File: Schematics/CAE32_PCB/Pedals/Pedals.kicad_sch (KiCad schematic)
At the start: 20 parts, among them J1 Conn_01x19_Pin, SW1 CONFIG, SW2 SW, SW3 SW, U1 STM32F072RBTx, Y1 Crystal_GND24_Small

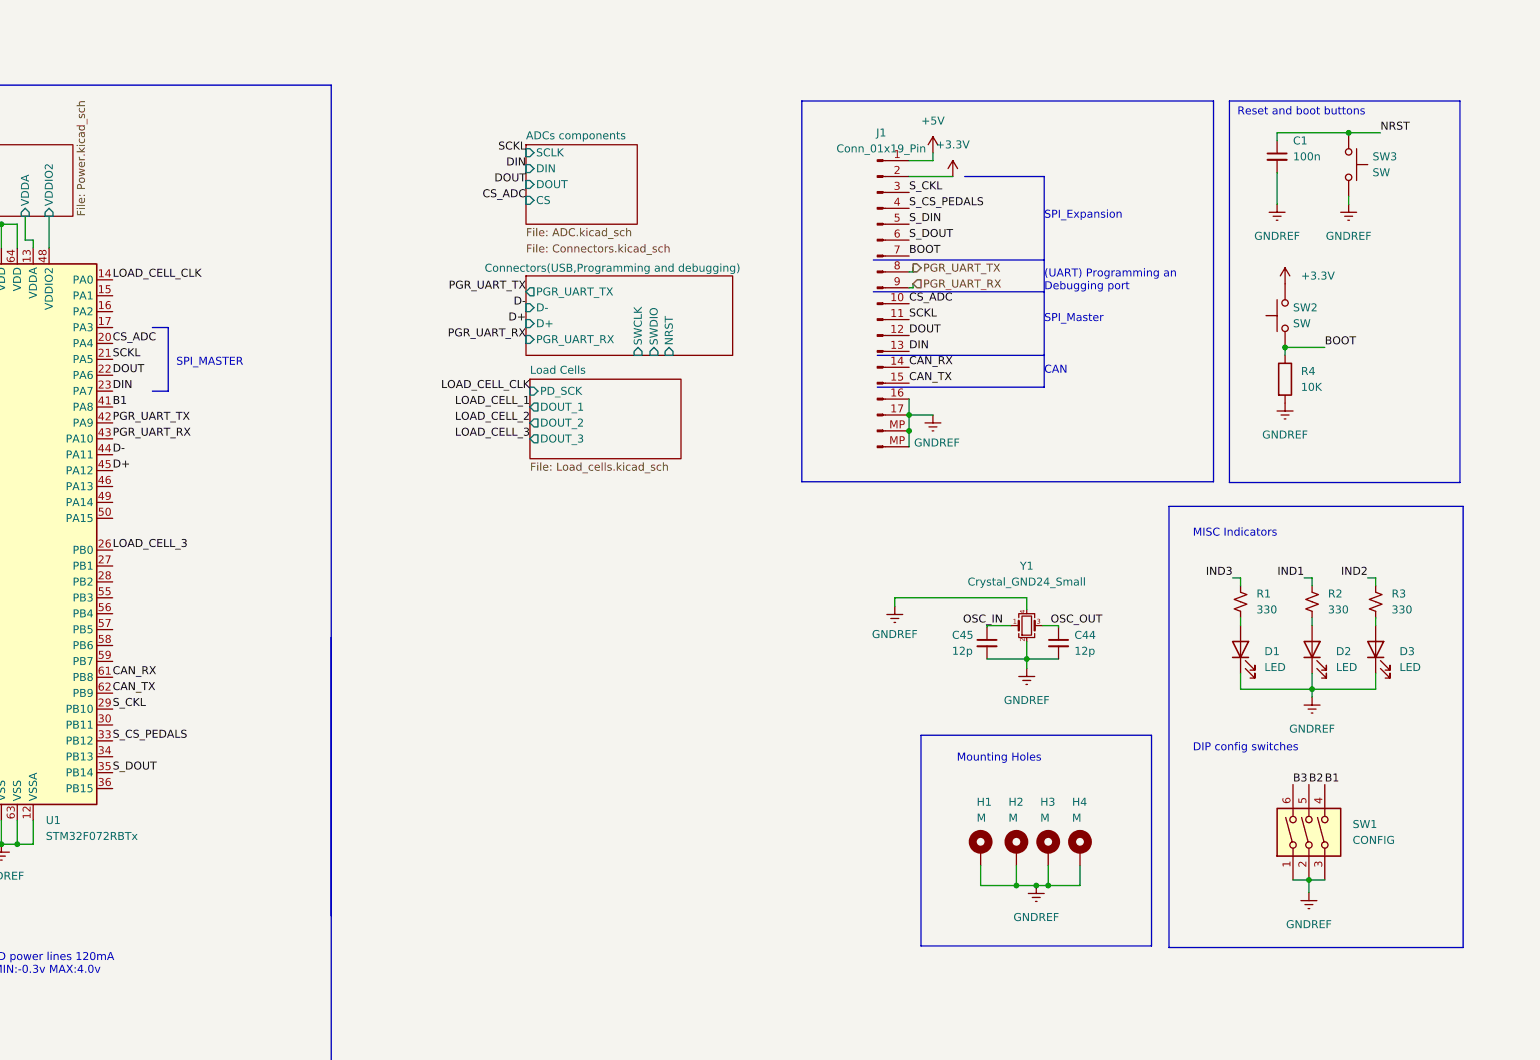
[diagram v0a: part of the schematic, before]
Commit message: updated: Pcb design, fixed plane grounds and minor improvements, added stlink connector, updated BOM with the current market stock
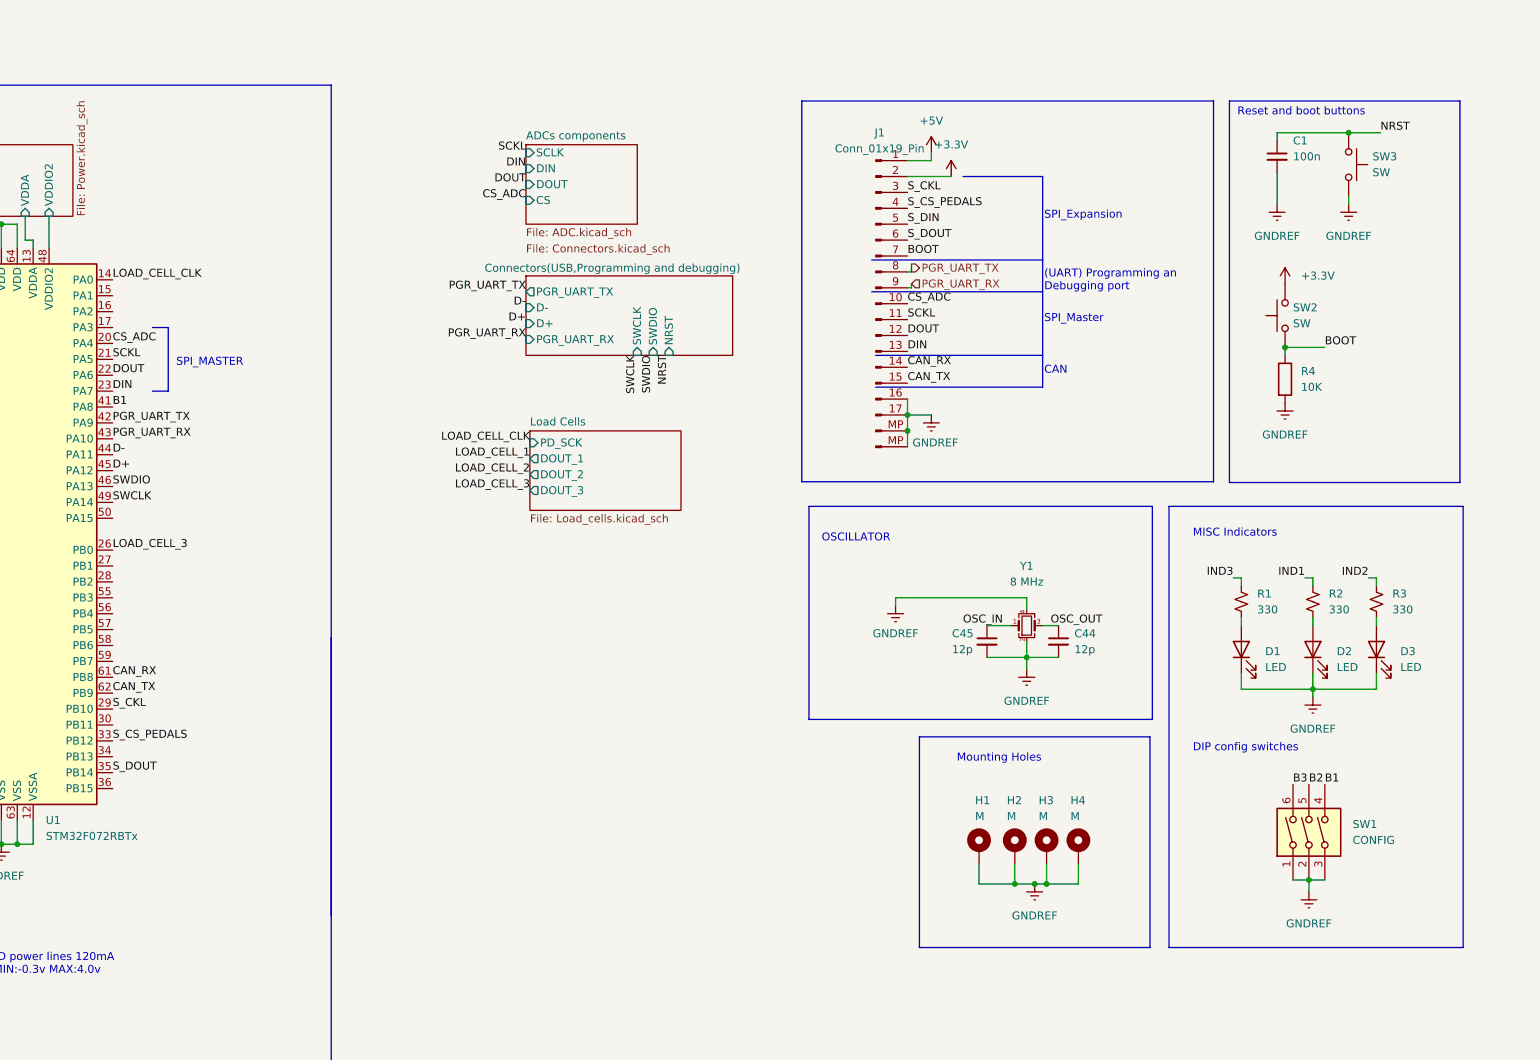
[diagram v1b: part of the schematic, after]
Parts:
- C1: Item c1591 -> C66501; LCSC_PART c1591 -> C66501; Vendor c1591 -> C66501
- R1, R2, R3: Item C25804 -> C21190; LCSC_PART C25804 -> C21190; Vendor C25804 -> C21190
- Y1: value Crystal_GND24_Small -> 8 MHz
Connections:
- net SWDIO: now reaches U1.46 (PA13)
- net SWCLK: now reaches U1.49 (PA14)
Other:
- note added: "OSCILLATOR"

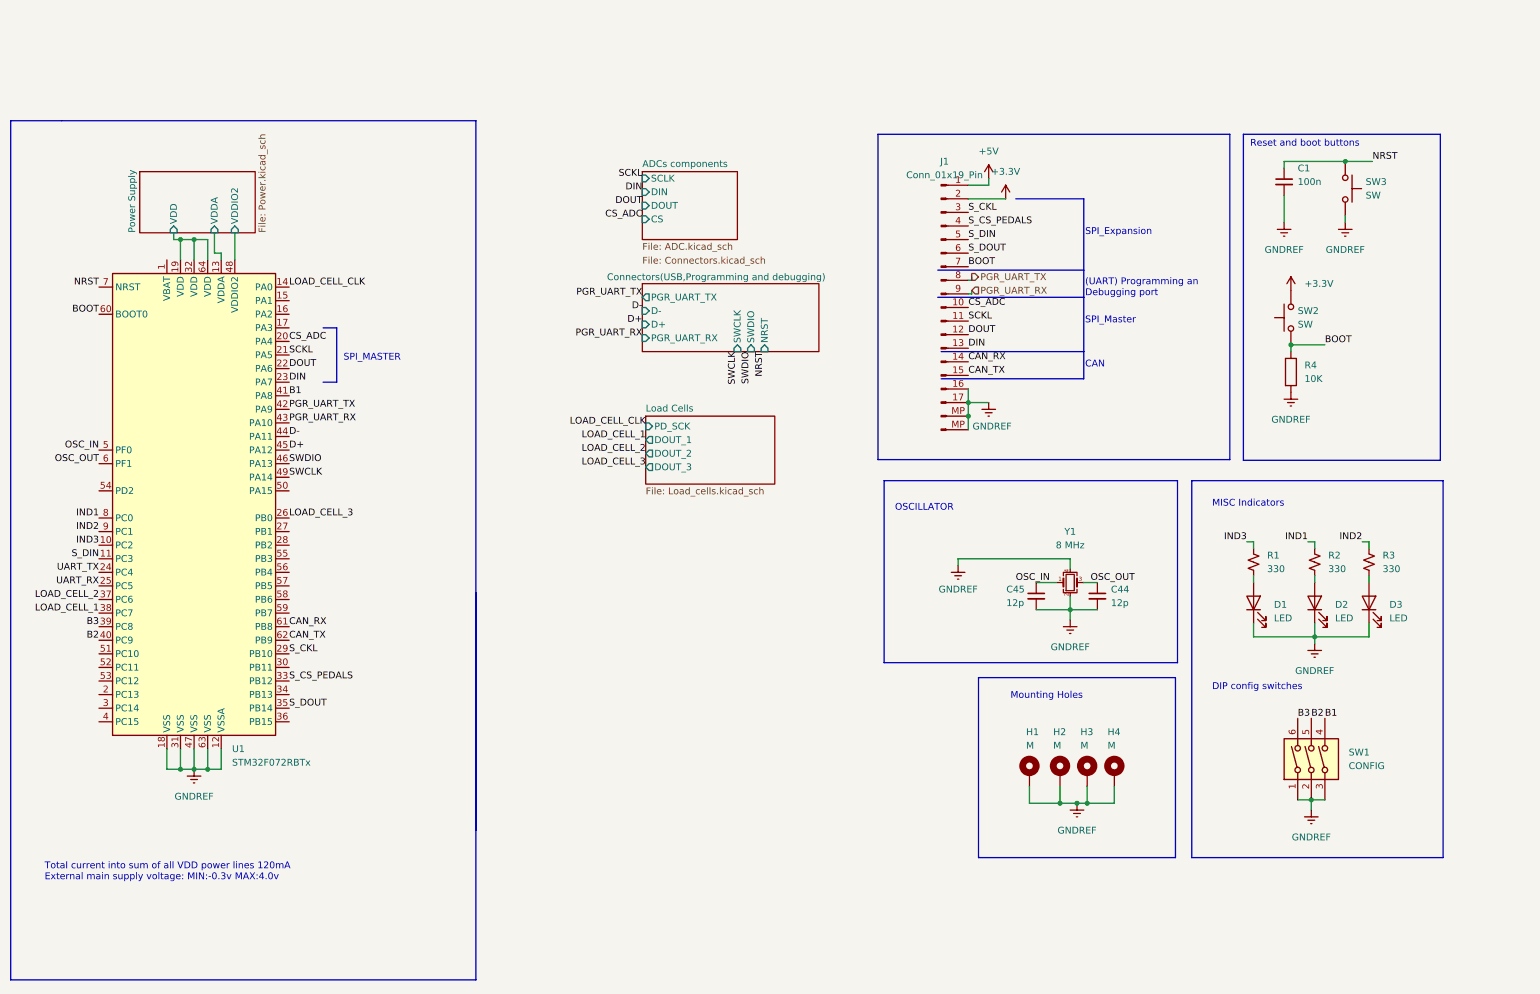
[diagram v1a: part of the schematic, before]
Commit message: fixed: SPI route
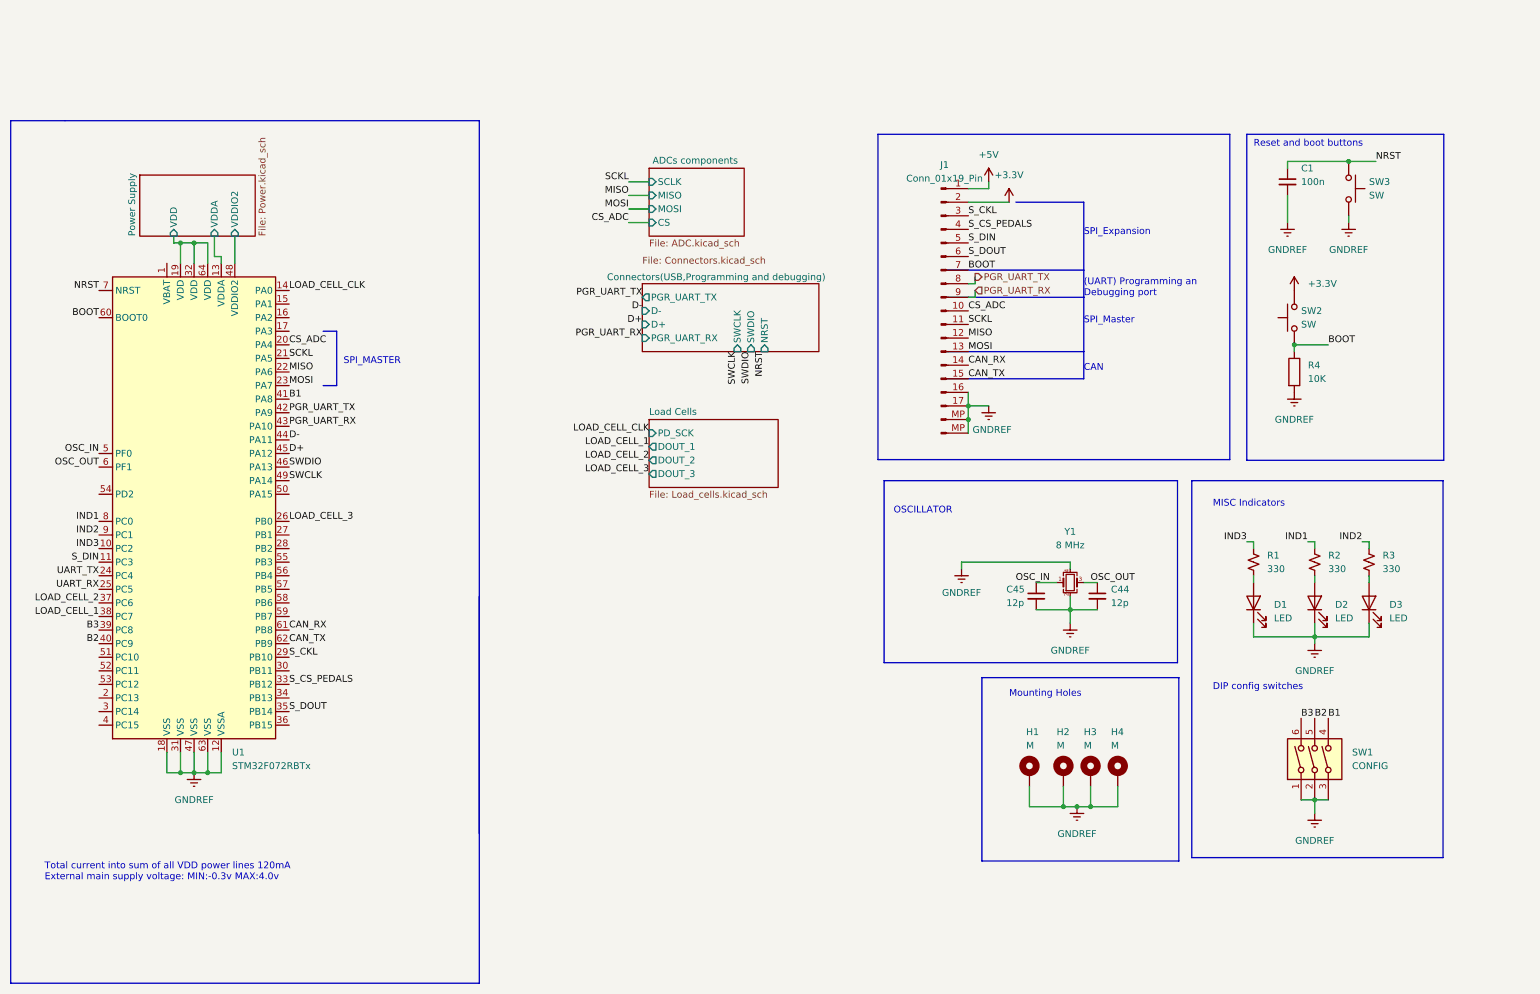
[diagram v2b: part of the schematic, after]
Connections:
- net DIN renamed MOSI
- net DOUT renamed MISO
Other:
- sheet ADCs components ports: added MISO, MOSI; removed DIN, DOUT
- moved on the sheet: C1, H2, H3, H4, J1, R4, SW1, SW2, SW3, U1

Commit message: fixed: SPI route and updated kicad versions in schematic and pcb design
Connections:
- no-connect marks 0 -> 24
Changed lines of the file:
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@@
 	(title_block
 		(title "CAE32 pedals")
-		(date "2024-01-13")
-		(rev "1")
+		(date "2025-07-05")
+		(rev "2")
 		(comment 1 "Desing by: janc18")
 		(comment 2 "Version 2.1")
@@
 		(color 0 0 0 0)
 	)
+	(no_connect
+		(at 30.48 116.84)
+	)
+	(no_connect
+		(at 66.04 104.14)
+	)
+	(no_connect
+		(at 30.48 124.46)
+	)
+	(no_connect
+		(at 66.04 53.34)
+	)
+	(no_connect
+		(at 30.48 86.36)
+	)
+	(no_connect
+		(at 30.48 127)
+	)
+	(no_connect
+		(at 43.18 43.18)
+	)
+	(no_connect
+		(at 66.04 96.52)
+	)
+	(no_connect
+		(at 66.04 129.54)
+	)
+	(no_connect
+		(at 66.04 124.46)
+	)
+	(no_connect
+		(at 66.04 109.22)
+	)
+	(no_connect
+		(at 66.04 55.88)
+	)
+	(no_connect
+		(at 66.04 101.6)
+	)
+	(no_connect
+		(at 30.48 129.54)
+	)
+	(no_connect
+		(at 66.04 99.06)
+	)
+	(no_connect
+		(at 66.04 86.36)
+	)
+	(no_connect
+		(at 66.04 93.98)
+	)
+	(no_connect
+		(at 27.94 104.14)
+	)
+	(no_connect
+		(at 27.94 101.6)
+	)
+	(no_connect
+		(at 30.48 121.92)
+	)
+	(no_connect
+		(at 66.04 119.38)
+	)
+	(no_connect
+		(at 30.48 119.38)
+	)
+	(no_connect
+		(at 66.04 50.8)
+	)
+	(no_connect
+		(at 66.04 106.68)
+	)
 	(wire
 		(pts
@@
 		)
 	)
+	(wire
+		(pts
+			(xy 27.94 104.14) (xy 30.48 104.14)
+		)
+		(stroke
+			(width 0)
+			(type default)
+		)
+	)
 	(polyline
 		(pts
@@
 		(pts
 			(xy 205.74 102.87) (xy 209.55 102.87)
+		)
+		(stroke
+			(width 0)
+			(type default)
+		)
+	)
+	(wire
+		(pts
+			(xy 27.94 101.6) (xy 30.48 101.6)
 		)
 		(stroke
@@
 	)
 	(label "UART_TX"
-		(at 30.48 101.6 180)
+		(at 27.94 101.6 180)
 		(effects
 			(font
@@
 	)
 	(label "UART_RX"
-		(at 30.48 104.14 180)
-		(effects
-			(font
-				(size 1.27 1.27)
-			)
-			(justify right bottom)
-		)
-	)
-	(label "S_CKL"
-		(at 516.89 -27.94 0)
-		(effects
-			(font
-				(size 1.27 1.27)
-			)
-			(justify left bottom)
-		)
-	)
+		(at 27.94 104.14 180)
+		(effects
+			(font
+				(size 1.27 1.27)
+			)
+			(justify right bottom)
+		)
+	)
